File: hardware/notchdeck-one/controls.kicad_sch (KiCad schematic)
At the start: 62 parts, among them J9 REV F-N-R, SW1 SW_Push, SW10 SW_Push, SW11 SW_Push, SW12 SW_Push, SW13 SW_Push, SW14 SW_Push, SW15 SW_Push, SW16 SW_Push, SW2 SW_Push, SW3 SW_Push, SW4 SW_Push, SW5 SW_Push, SW6 SW_Push, SW7 SW_Push, SW8 SW_Push, SW9 SW_Push, U8 74AHCT1G125

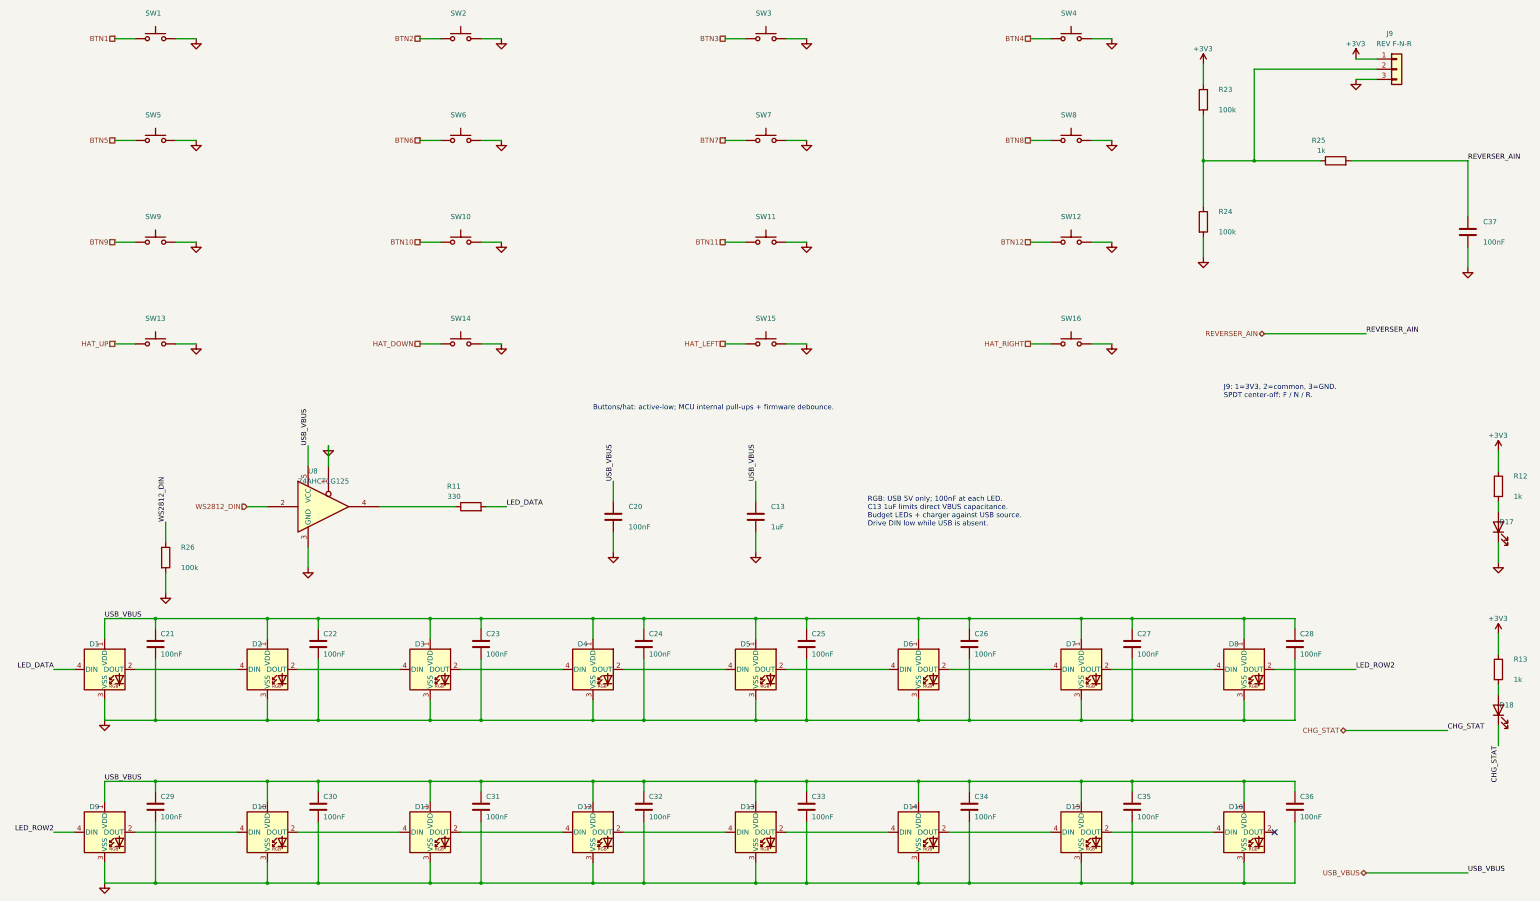
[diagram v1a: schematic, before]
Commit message: Split controller buttons onto stocked STM32G030 panel PCB
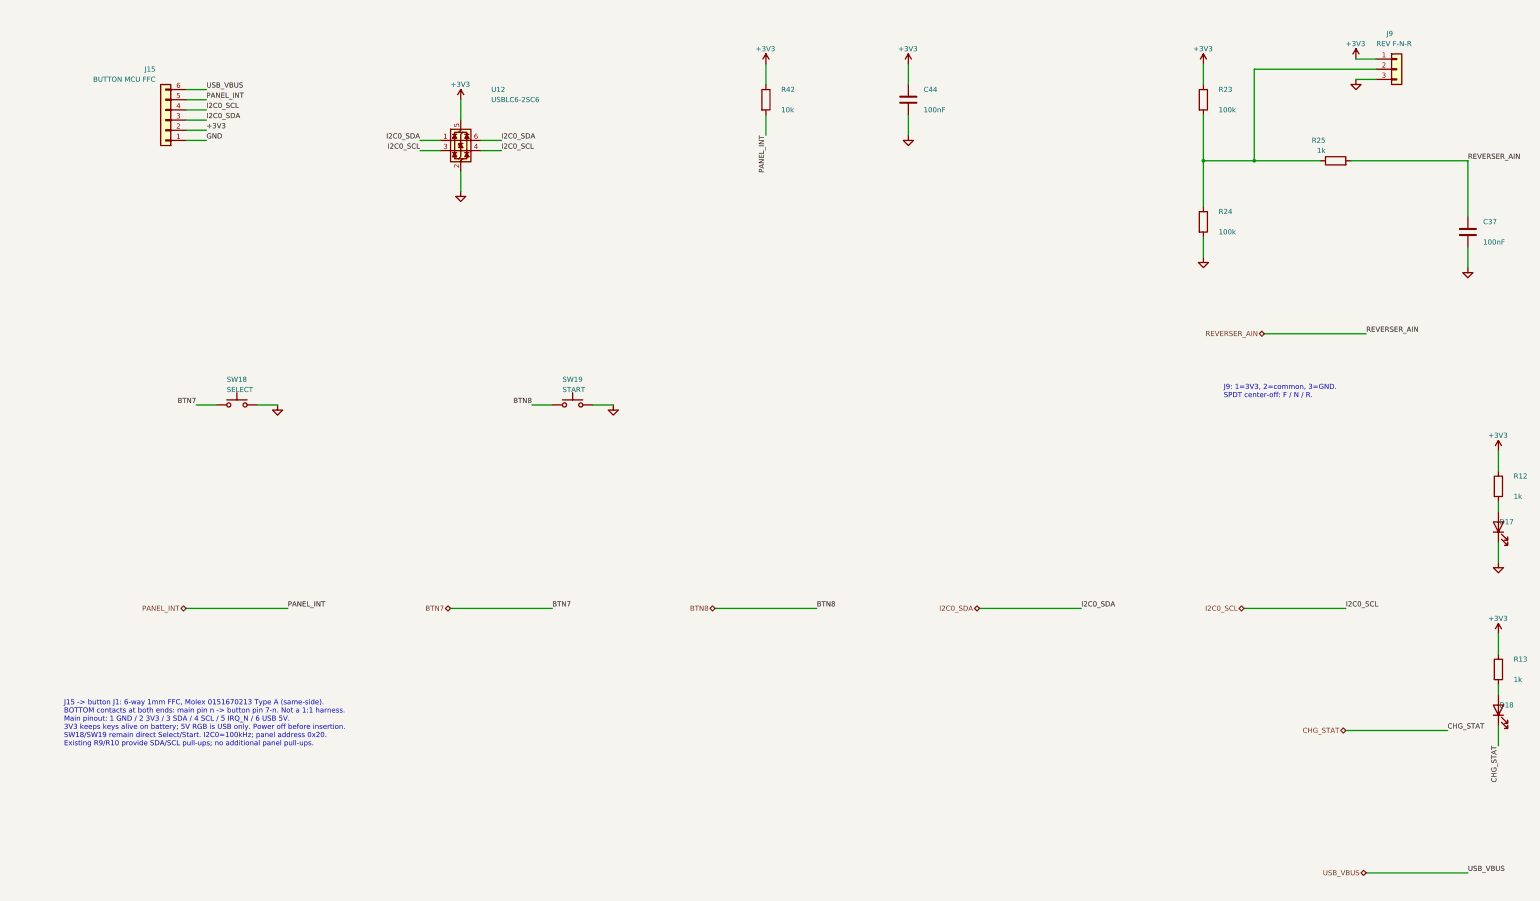
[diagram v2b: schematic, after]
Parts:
- removed C13: 1uF, Capacitor_SMD:C_0805_2012Metric, symbol Device:C
- removed C20, C21, C22, C23, C24, C25, C26, C27, C28, C29, C30, C31, C32, C33, C34, C35, C36: 100nF, Capacitor_SMD:C_0402_1005Metric, symbol Device:C
- removed D1, D10, D11, D12, D13, D14, D15, D16, D2, D3, D4, D5, D6, D7, D8, D9: WS2812B, notchdeck:LED_XINGLIGHT_XL-5050RGBC-2812B, symbol LED:WS2812B
- removed R11: 330, Resistor_SMD:R_0402_1005Metric, symbol Device:R
- removed R26: 100k, Resistor_SMD:R_0402_1005Metric, symbol Device:R
- removed SW1, SW10, SW11, SW12, SW13, SW14, SW15, SW16, SW2, SW3, SW4, SW5, SW6, SW7, SW8, SW9: SW_Push, Button_Switch_SMD:SW_Push_1P1T_XKB_TS-1187A, symbol Switch:SW_Push
- removed U8: 74AHCT1G125, Package_TO_SOT_SMD:SOT-23-5, symbol 74xGxx:74AHCT1G125
- added C44: 100nF, Capacitor_SMD:C_0402_1005Metric, symbol Device:C
- added J15: BUTTON MCU FFC, Connector_FFC-FPC:JUSHUO_AFA07-S06FCA-00_1x6-1MP_P1.0mm_Horizontal, symbol Connector_Generic:Conn_01x06
- added R42: 10k, Resistor_SMD:R_0402_1005Metric, symbol Device:R
- added SW18: SELECT, Button_Switch_SMD:SW_Push_1P1T_XKB_TS-1187A, symbol Switch:SW_Push
- added SW19: START, Button_Switch_SMD:SW_Push_1P1T_XKB_TS-1187A, symbol Switch:SW_Push
- added U12: USBLC6-2SC6, Package_TO_SOT_SMD:SOT-23-6, symbol Power_Protection:USBLC6-2SC6
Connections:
- net +3V3: now also C44.1, J15.2 (Pin_2), R42.1, U12.5 (VBUS)
- net BTN7: now also SW18.1
- net BTN8: now also SW19.1
- net GND: now also C44.2, J15.1 (Pin_1), SW18.2, SW19.2, U12.2 (GND)
- net USB_VBUS: now also J15.6 (Pin_6)
- new net I2C0_SCL: J15.4 (Pin_4), U12.3 (I/O2), U12.4 (I/O2)
- new net I2C0_SDA: J15.3 (Pin_3), U12.1 (I/O1), U12.6 (I/O1)
- new net PANEL_INT: J15.5 (Pin_5), R42.2
- no-connect marks 1 -> 0
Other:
- note added: "J15 -> button J1: 6-way 1mm FFC, Molex 0151670213 Type A (same-side). BOTTOM contacts at both ends: main pin n -> button pin 7-n. Not a 1:1 harness. Main pinout: 1 GND / 2 3V3 / 3 SDA / 4 SCL / 5 IRQ_N / 6 USB 5V. 3V3 keeps keys alive on battery; 5V RGB is USB only. Power off before insertion. SW18/SW19 remain direct Select/Start. I2C0=100kHz; panel address 0x20. Existing R9/R10 provide SDA/SCL p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"
- note removed: "Buttons/hat: active-low; MCU internal pull-ups + firmware debounce."
- note removed: "RGB: USB 5V only; 100nF at each LED. C13 1uF limits direct VBUS capacitance. Budget LEDs + charger against USB source. Drive DIN low while USB is absent."
